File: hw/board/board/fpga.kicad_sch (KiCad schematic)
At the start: 1 part

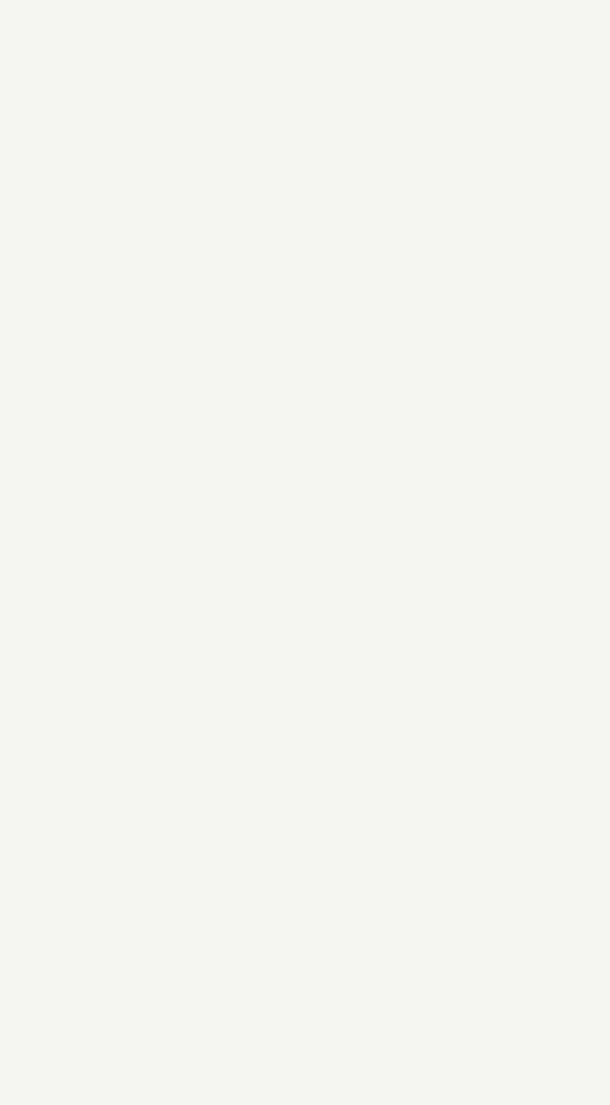
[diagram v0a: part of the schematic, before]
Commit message: Add wires to fpga block (but don't connect them)
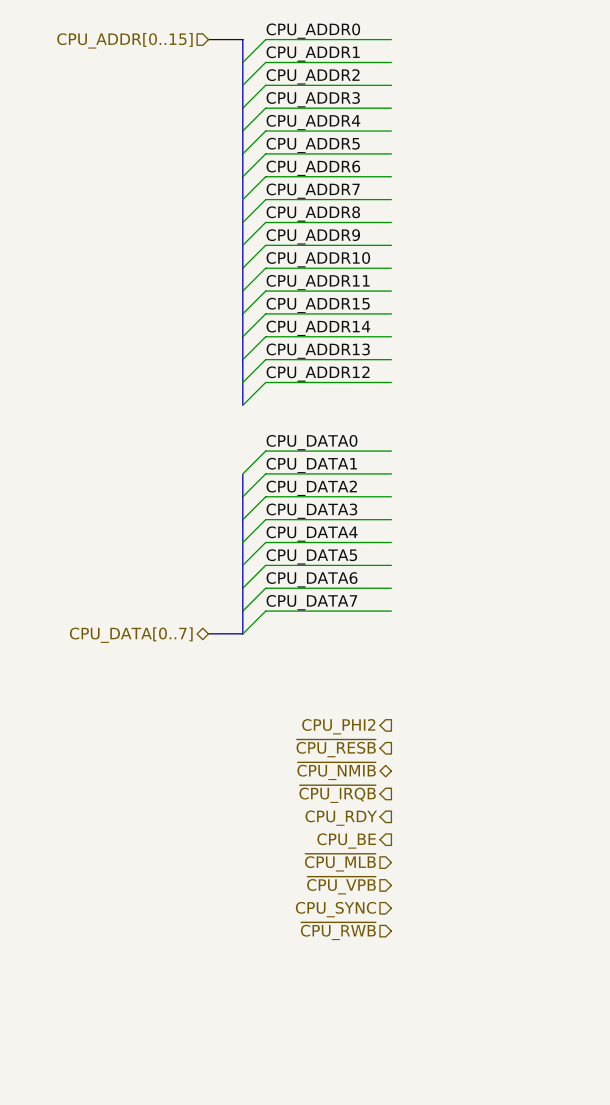
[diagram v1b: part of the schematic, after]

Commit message: Start work on ddr
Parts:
- added R46: 240R, Resistor_SMD:R_0402_1005Metric, symbol Device:R
- added unit 11 of U1
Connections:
- new net: R46.1, U1.Y5 (DDR_ZQ)
- new net +1V35: U1.L7 (VCCIO_DDR), U1.N7 (VCCIO_DDR), U1.P5 (VCCIO_DDR), U1.R2 (VCCIO_DDR), U1.R7 (VCCIO_DDR), U1.W4 (VCCIO_DDR)
- new net DDR_A0: U1.U4 (DDR_A0)
- new net DDR_A1: U1.W5 (DDR_A1)
- new net DDR_A10: U1.R5 (DDR_A10)
- new net DDR_A11: U1.N5 (DDR_A11)
- new net DDR_A12: U1.P4 (DDR_A12)
- new net DDR_A13: U1.M6 (DDR_A13)
- new net DDR_A14: U1.N4 (DDR_A14)
- new net DDR_A2: U1.V5 (DDR_A2)
- new net DDR_A3: U1.T6 (DDR_A3)
- new net DDR_A4: U1.T3 (DDR_A4)
- new net DDR_A5: U1.T5 (DDR_A5)
- new net DDR_A6: U1.T4 (DDR_A6)
- new net DDR_A7: U1.T1 (DDR_A7)
- new net DDR_A8: U1.R1 (DDR_A8)
- new net DDR_A9: U1.T2 (DDR_A9)
- new net DDR_BA0: U1.K3 (DDR_BA0)
- new net DDR_BA1: U1.K2 (DDR_BA2)
- new net DDR_BA2: U1.K1 (DDR_BA2)
- new net DDR_CAS#: U1.P6 (DDR_CAS_N)
- new net DDR_CK: U1.R3 (DDR_CK)
- new net DDR_CK#: U1.R4 (DDR_CK_N)
- new net DDR_CKE: U1.N6 (DDR_CKE)
- new net DDR_CS#: U1.R6 (DDR_CS_N)
- new net DDR_DM: U1.W1 (DDR_DM0)
- new net DDR_DQ0: U1.U3 (DDR_DQ0)
- new net DDR_DQ1: U1.W3 (DDR_DQ1)
- new net DDR_DQ2: U1.V3 (DDR_DQ2)
- new net DDR_DQ3: U1.U2 (DDR_DQ3)
- new net DDR_DQ4: U1.W2 (DDR_DQ4)
- new net DDR_DQ5: U1.Y3 (DDR_DQ5)
- new net DDR_DQ6: U1.Y4 (DDR_DQ6)
- new net DDR_DQ7: U1.Y2 (DDR_DQ7)
- new net DDR_DQS: U1.V1 (DDR_DQS0)
- new net DDR_DQS#: U1.U1 (DDR_DQS_N0)
- new net DDR_ODT: U1.L6 (DDR_ODT)
- new net DDR_RAS#: U1.M4 (DDR_RAS_N)
- new net DDR_RESET#: U1.L4 (DDR_RST_N)
- new net DDR_WE#: U1.K4 (DDR_WE_N)
- new net GND: R46.2
- new net VTT: U1.V4 (DDR_VREF)

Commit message: Add decoupling capacitors
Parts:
- added U17: ~, Package_SO:SOP-8_3.9x4.9mm_P1.27mm, symbol IC:MX25V8035F
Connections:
- no-connect marks 0 -> 12
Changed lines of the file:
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@@
   (junction (at 100.33 237.49) (diameter 0) (color 0 0 0 0)
   )
+  (no_connect (at 102.87 339.09))
+  (no_connect (at 102.87 344.17))
+  (no_connect (at 102.87 351.79))
+  (no_connect (at 102.87 334.01))
+  (no_connect (at 102.87 311.15))
+  (no_connect (at 102.87 285.75))
+  (no_connect (at 102.87 341.63))
+  (no_connect (at 102.87 349.25))
+  (no_connect (at 102.87 336.55))
+  (no_connect (at 102.87 356.87))
+  (no_connect (at 102.87 346.71))
+  (no_connect (at 102.87 361.95))
   (bus_entry (at 85.09 257.81) (size -2.54 2.54)
     (stroke (width 0) (type default))
@@
         )
       )
+    )
+  )
+  (symbol (lib_id "IC:MX25V8035F") (at 132.08 128.27 0) (unit 1)
+    (in_bom yes) (on_board yes) (dnp no) (fields_autoplaced)
+    (property "Reference" "U17" (at 142.875 124.46 0)
+      (effects (font (size 1.27 1.27)))
+    )
+    (property "Value" "~" (at 132.08 128.27 0)
+      (effects (font (size 1.27 1.27)))
+    )
+    (property "Footprint" "Package_SO:SOP-8_3.9x4.9mm_P1.27mm" (at 142.875 127 0)
+      (effects (font (size 1.27 1.27)))
+    )
+    (property "Datasheet" "" (at 132.08 128.27 0)
+      (effects (font (size 1.27 1.27)) hide)
+    )
+    (pin "1")
+    (pin "2")
+    (pin "3")
+    (pin "4")
+    (pin "5")
+    (pin "6")
+    (pin "7")
+    (pin "8")
+    (instances
+      (project "board"
+        (path "/0c7bd276-5f73-4ef8-a8a2-874fce123825/95d69960-5749-4bf0-ba13-8cc427d1e8e9"
+          (reference "U17") (unit 1)
+        )
+        (path "/0c7bd276-5f73-4ef8-a8a2-874fce123825/40603e20-84c6-45bc-99e6-f7272e6c1ac0"
+          (reference "U16") (unit 1)
+        )
+      )
